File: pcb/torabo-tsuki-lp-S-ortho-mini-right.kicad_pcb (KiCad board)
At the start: 2 copper layers, 128.5 x 74 mm, 57 parts, among them J201 Conn_01x06_MountingPin, J202 FTSH-106-01-L-D-K, SW43 SW_Push, SW44 SW_Push, SW45 SW_Push, SW46 SW_Push, SW47 SW_Push, SW48 SW_Push, SW50 SW_Push, SW51 SW_Push, SW52 SW_Push, SW53 SW_Push, SW54 SW_Push, SW55 SW_Push, SW57 SW_Push, SW58 SW_Push, SW59 SW_Push, SW60 SW_Push, SW61 SW_Push, SW62 SW_Push, SW64 SW_Push, SW65 SW_Push, SW69 SW_Push, SW70 SW_Push, U201 XIAO nRF52840 Plus

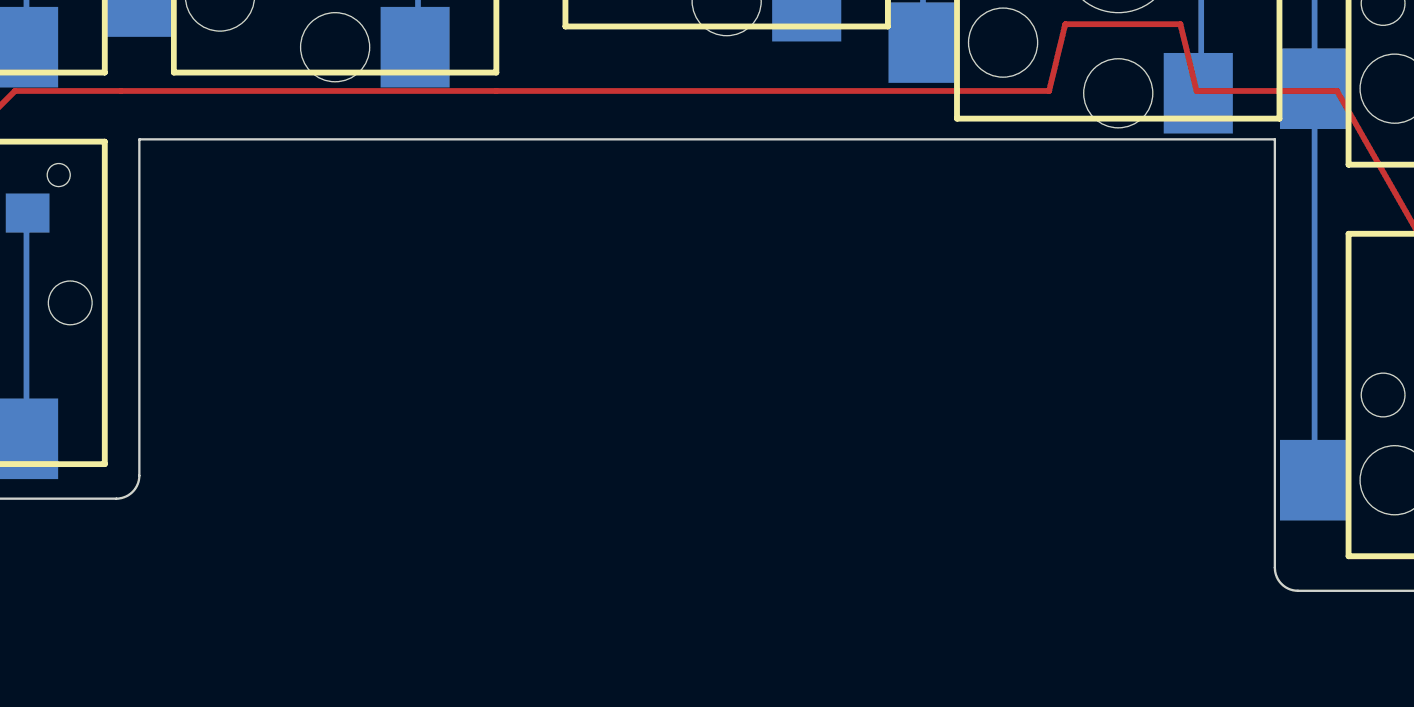
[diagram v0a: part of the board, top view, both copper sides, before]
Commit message: Fit right PCB outline around inner key
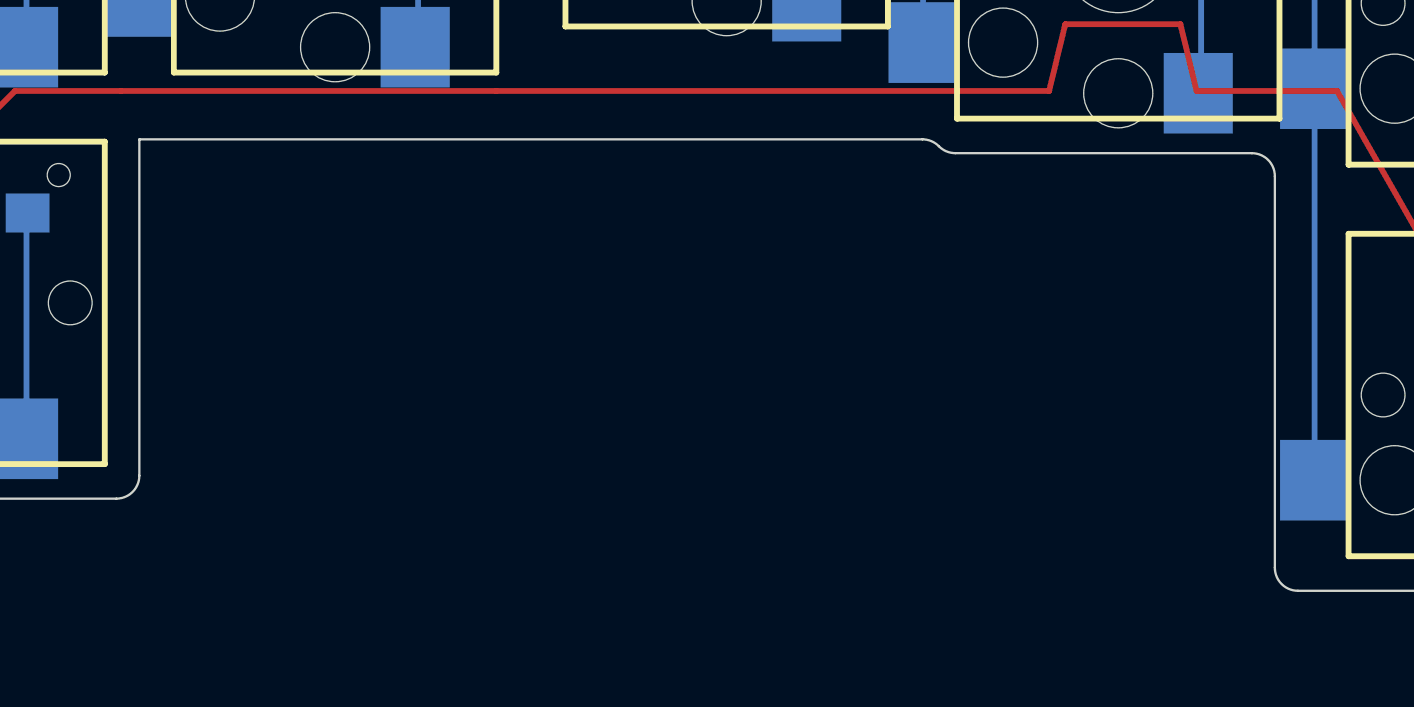
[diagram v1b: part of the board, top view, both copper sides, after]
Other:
- outline, holes or cut-outs redrawn
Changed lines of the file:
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@@
 	)
 	(gr_line
-		(start 128.6 169.9)
+		(start 113.3 169.9)
 		(end 79.3 169.9)
+		(stroke
+			(width 0.1)
+			(type default)
+		)
+		(layer "Edge.Cuts")
+	)
+	(gr_arc
+		(start 113.3 169.9)
+		(mid 113.687 169.978)
+		(end 114.014 170.2)
+		(stroke
+			(width 0.1)
+			(type default)
+		)
+		(layer "Edge.Cuts")
+	)
+	(gr_arc
+		(start 114.014 170.2)
+		(mid 114.341 170.422)
+		(end 114.728 170.5)
+		(stroke
+			(width 0.1)
+			(type default)
+		)
+		(layer "Edge.Cuts")
+	)
+	(gr_line
+		(start 114.728 170.5)
+		(end 127.6 170.5)
+		(stroke
+			(width 0.1)
+			(type default)
+		)
+		(layer "Edge.Cuts")
+	)
+	(gr_arc
+		(start 128.6 171.5)
+		(mid 128.307107 170.792893)
+		(end 127.6 170.5)
 		(stroke
 			(width 0.1)
@@
 	(gr_line
 		(start 128.6 188.5)
-		(end 128.6 169.9)
+		(end 128.6 171.5)
 		(stroke
 			(width 0.1)

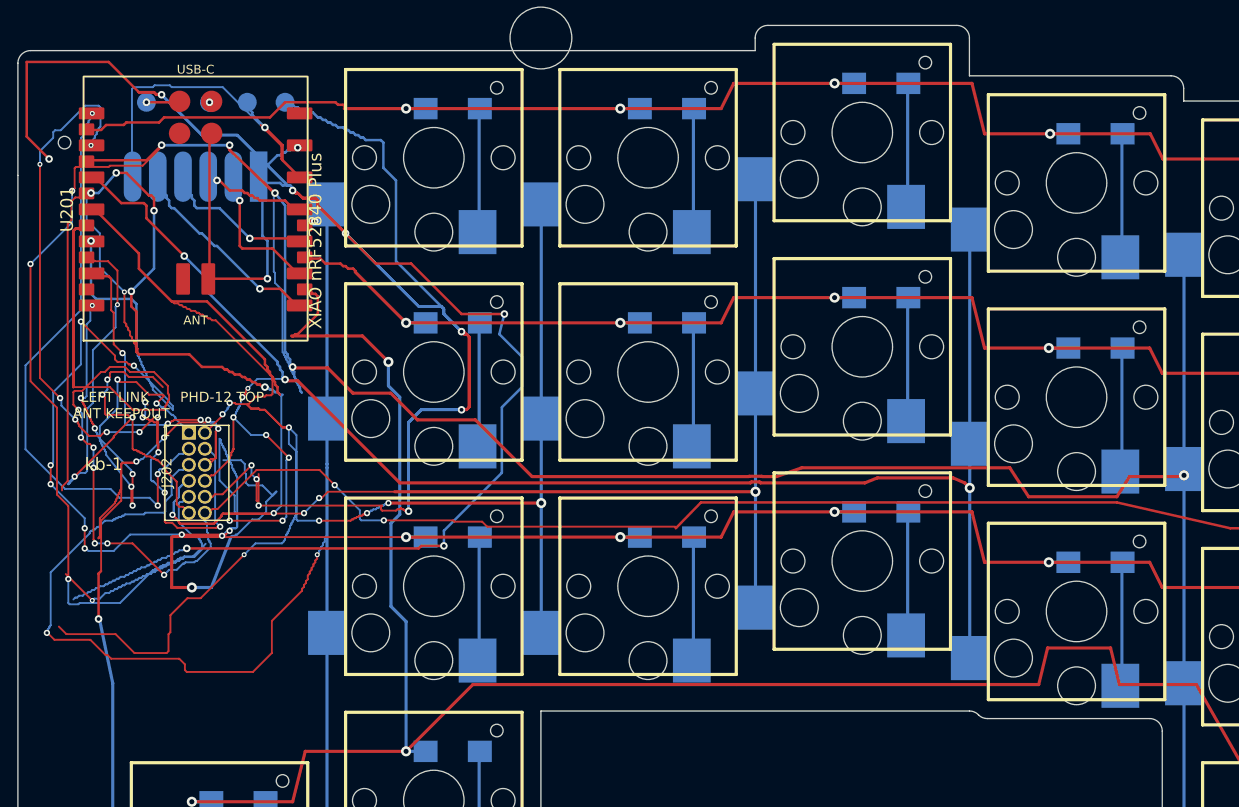
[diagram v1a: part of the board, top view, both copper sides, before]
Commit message: Improve XIAO and trackball adapter solder access
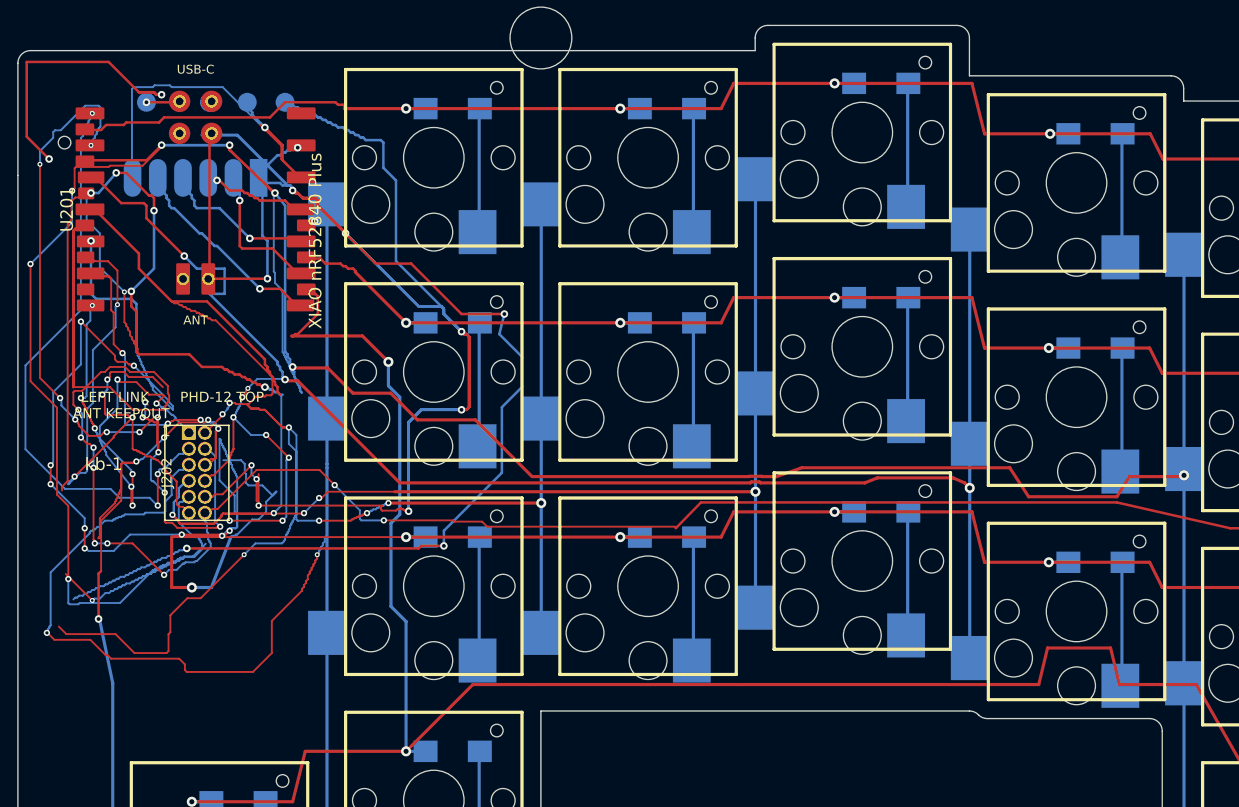
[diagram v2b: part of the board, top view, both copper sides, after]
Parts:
- moved J201 0.10 mm to (51.9, 127.6)
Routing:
- net GND: track 298.3 -> 289.2 mm
- net /right/COL2: track 143.5 -> 146.4 mm
- net /right/SWDCLK: track 0.28 -> 0.00 mm, vias 1 -> 0

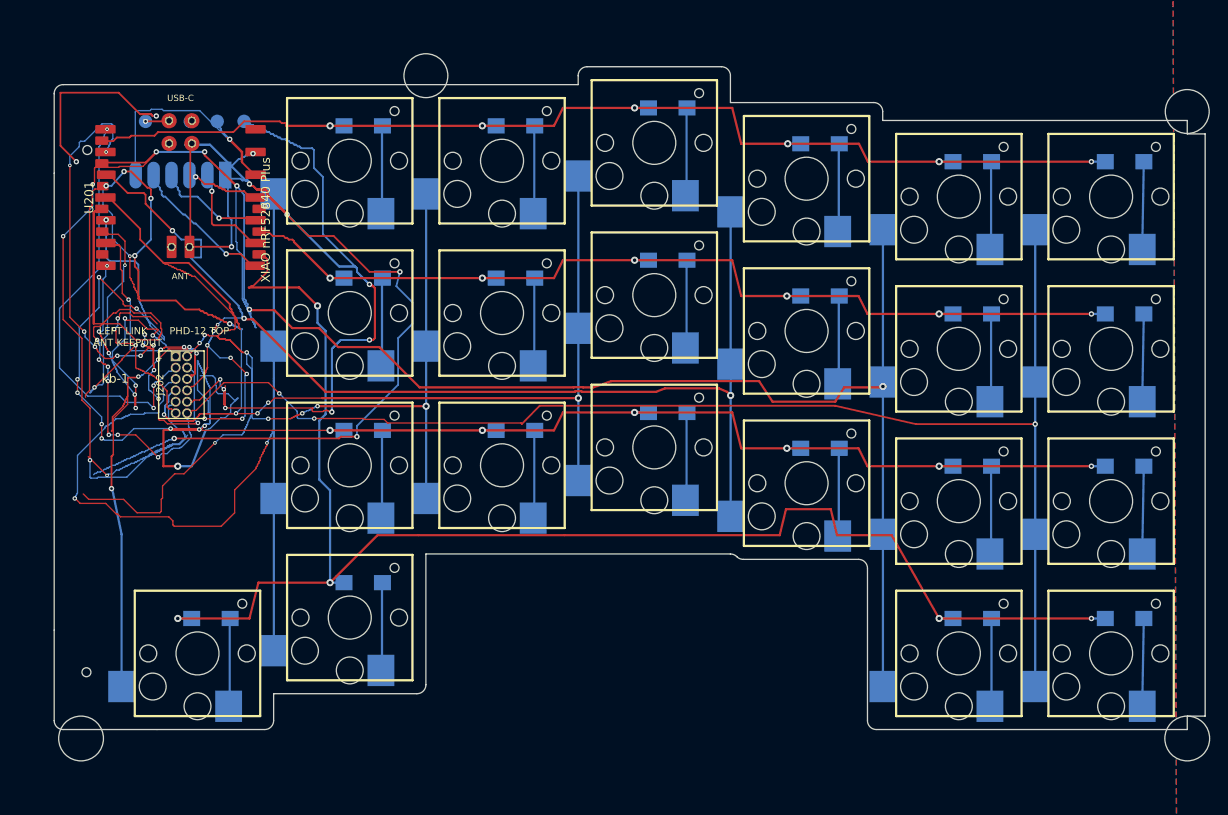
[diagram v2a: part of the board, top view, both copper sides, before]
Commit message: Add routed screw reliefs to both PCBs and panel
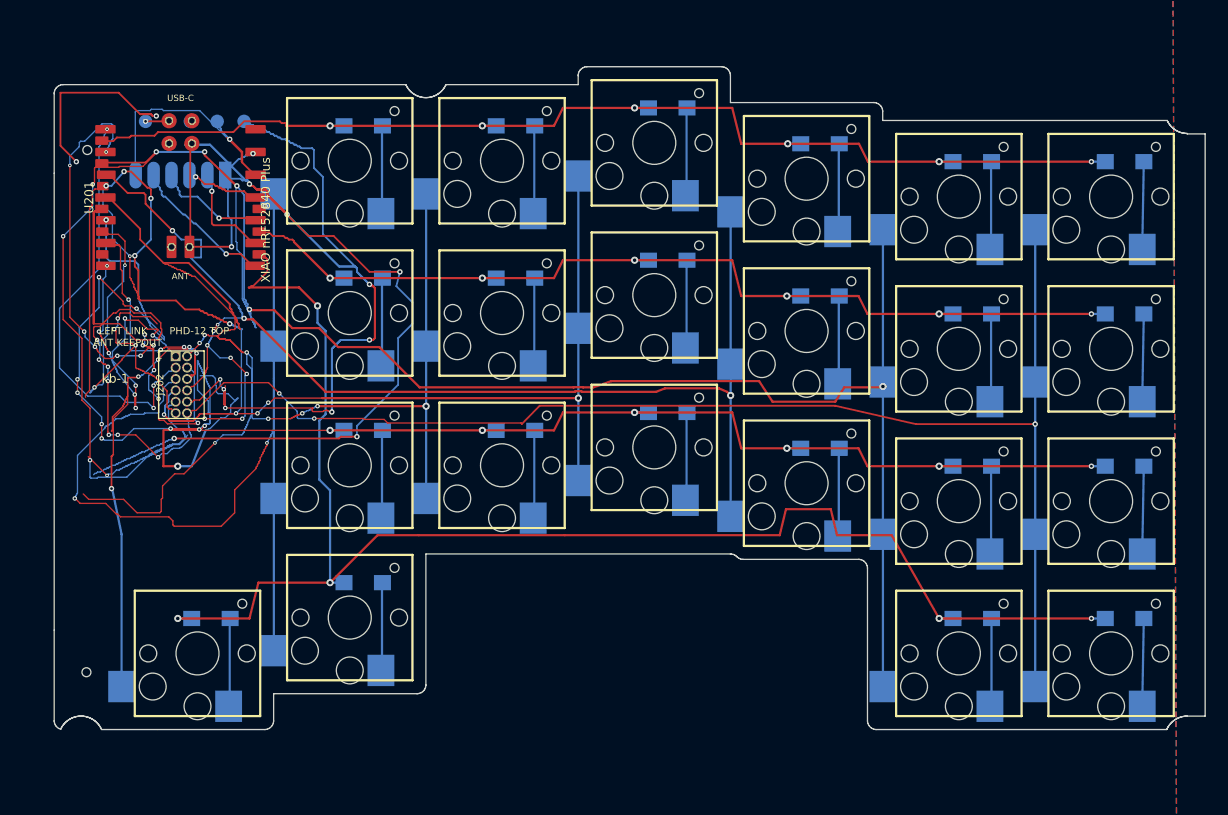
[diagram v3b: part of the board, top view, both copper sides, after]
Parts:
- removed the REF** at (79.3, 116.5)
- removed the REF** at (164.3, 190.5)
- removed the REF** at (40.8, 190.5)
- removed the REF** at (164.3, 120.5)
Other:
- outline, holes or cut-outs redrawn

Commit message: Rename keyboard to FORT-48
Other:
- board text added: "FORT-48"
- board text removed: "kb-1"
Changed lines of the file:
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@@
 		)
 	)
-	(gr_text "kb-1"
-		(at 43.1 150.9 0)
+	(gr_text "FORT-48"
+		(at 40.1 150.9 0)
 		(layer "F.SilkS")
 		(effects

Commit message: Rename keyboard to komoro (#54)
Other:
- board text added: "komoro"
- board text removed: "FORT-48"
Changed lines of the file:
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@@
 		)
 	)
-	(gr_text "FORT-48"
+	(gr_text "komoro"
 		(at 40.1 150.9 0)
 		(layer "F.SilkS")
